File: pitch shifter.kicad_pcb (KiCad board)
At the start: 2 copper layers, 53.8 x 62.2 mm, 7 parts, among them J1 MOLEX_430450412, J2 MOLEX_436500315, U1 AP63200WU-7, U2 STM32G030K8T6, U3 PCM3060PWR, U4 LMV321LILT

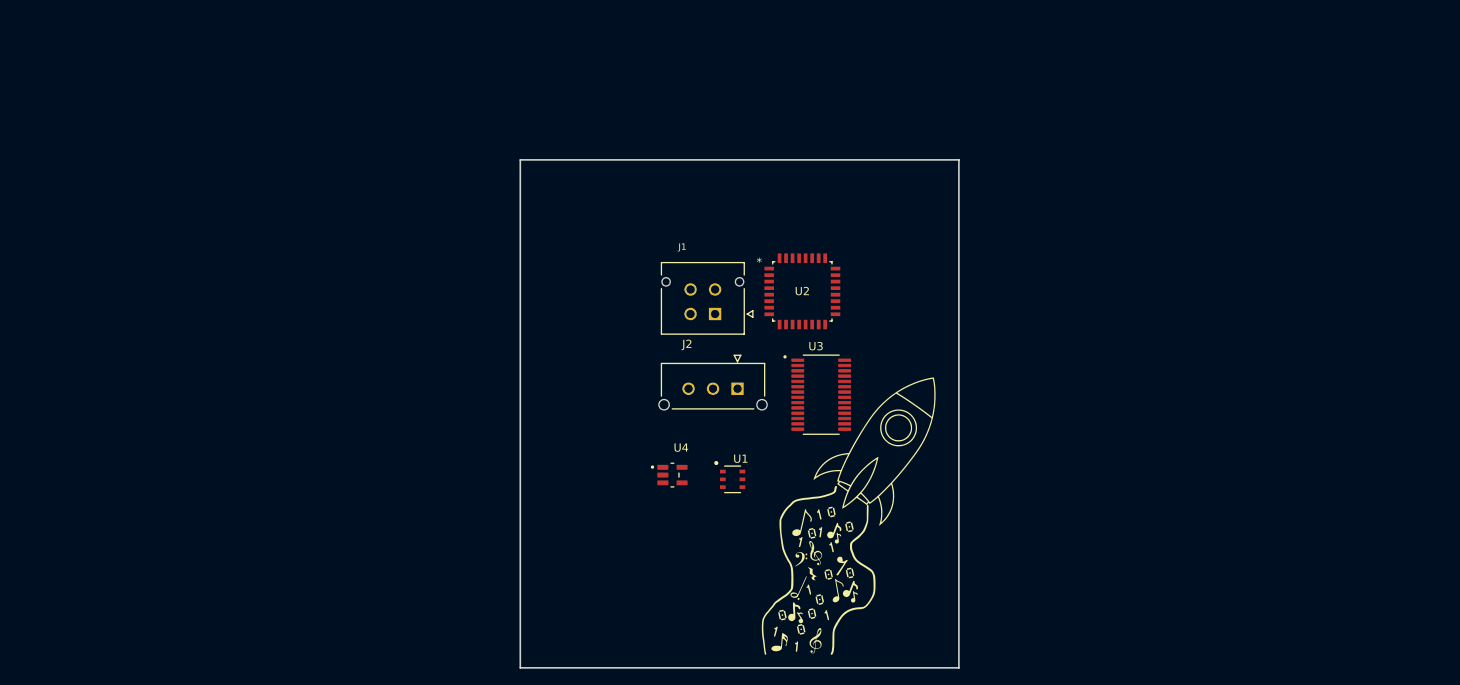
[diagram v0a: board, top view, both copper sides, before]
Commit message: Add oscillator, mounting holes, switches
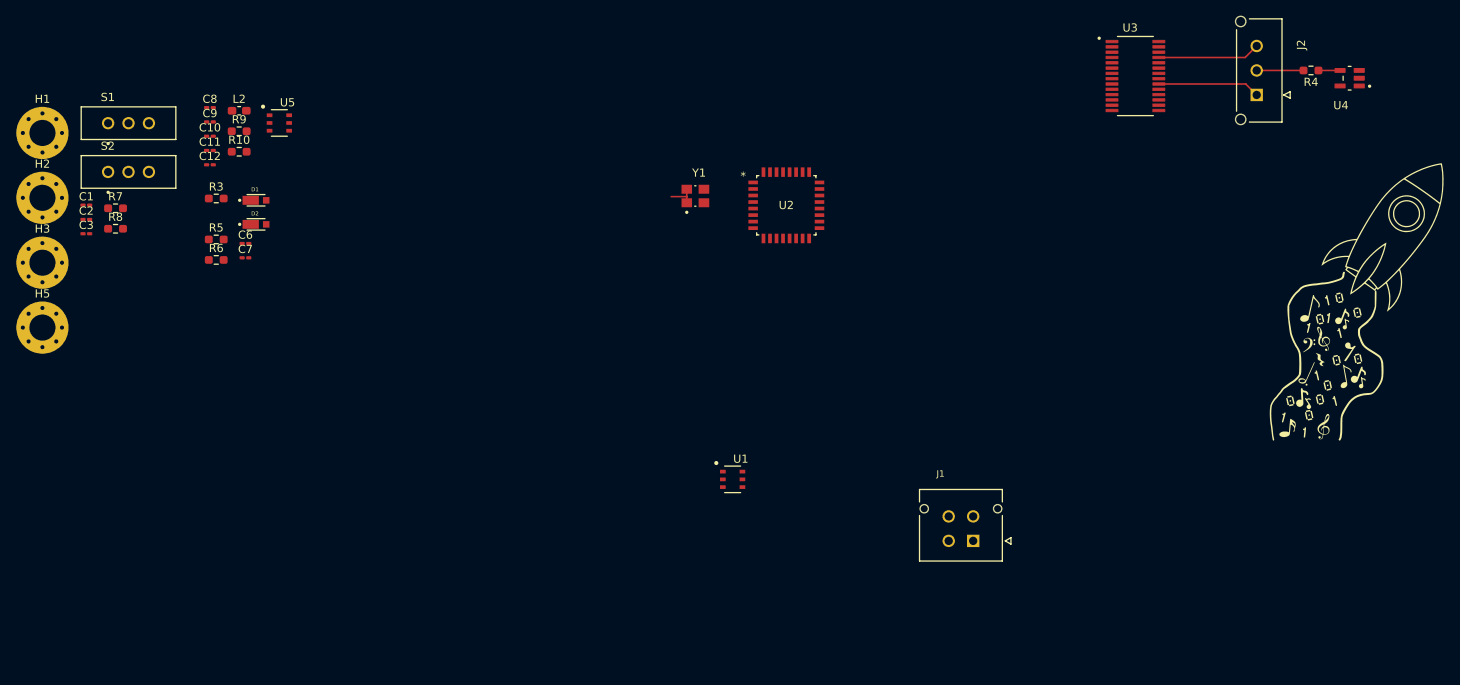
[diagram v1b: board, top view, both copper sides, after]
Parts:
- added C1: 100n, Capacitor_SMD:C_0201_0603Metric_Pad0.64x0.40mm_HandSolder, F.Cu at (64.6, 58.3)
- added C10: 100p, Capacitor_SMD:C_0201_0603Metric_Pad0.64x0.40mm_HandSolder, F.Cu at (79.7, 49.9)
- added C11: 22u, Capacitor_SMD:C_0201_0603Metric_Pad0.64x0.40mm_HandSolder, F.Cu at (79.7, 51.6)
- added C12: 22u, Capacitor_SMD:C_0201_0603Metric_Pad0.64x0.40mm_HandSolder, F.Cu at (79.7, 53.4)
- added C2: 100n, Capacitor_SMD:C_0201_0603Metric_Pad0.64x0.40mm_HandSolder, F.Cu at (64.6, 60.0)
- added C3: 100n, Capacitor_SMD:C_0201_0603Metric_Pad0.64x0.40mm_HandSolder, F.Cu at (64.6, 61.8)
- added C6: 100n, Capacitor_SMD:C_0201_0603Metric_Pad0.64x0.40mm_HandSolder, F.Cu at (84.1, 63.0)
- added C7: 100p, Capacitor_SMD:C_0201_0603Metric_Pad0.64x0.40mm_HandSolder, F.Cu at (84.1, 64.8)
- added C8: 10u, Capacitor_SMD:C_0201_0603Metric_Pad0.64x0.40mm_HandSolder, F.Cu at (79.7, 46.4)
- added C9: 100n, Capacitor_SMD:C_0201_0603Metric_Pad0.64x0.40mm_HandSolder, F.Cu at (79.7, 48.1)
- added D1: MSS1P4-M3_89A, Project_Components:MSS1P4-M3_89A, F.Cu at (85.4, 57.7)
- added D2: MSS1P4-M3_89A, Project_Components:MSS1P4-M3_89A, F.Cu at (85.4, 60.6)
- added H1: MountingHole_Pad, MountingHole:MountingHole_3.2mm_M3_Pad_Via, F.Cu at (59.2, 49.5)
- added H2: MountingHole_Pad, MountingHole:MountingHole_3.2mm_M3_Pad_Via, F.Cu at (59.2, 57.4)
- added H3: MountingHole_Pad, MountingHole:MountingHole_3.2mm_M3_Pad_Via, F.Cu at (59.2, 65.3)
- added H5: MountingHole_Pad, MountingHole:MountingHole_3.2mm_M3_Pad_Via, F.Cu at (59.2, 73.3)
- added L2: 6.8u, Inductor_SMD:L_0603_1608Metric_Pad1.05x0.95mm_HandSolder, F.Cu at (83.3, 46.7)
- added R10: 62K, Resistor_SMD:R_0603_1608Metric_Pad0.98x0.95mm_HandSolder, F.Cu at (83.3, 51.8)
- added R3: 100k, Resistor_SMD:R_0603_1608Metric_Pad0.98x0.95mm_HandSolder, F.Cu at (80.5, 57.5)
- added R4: 100k, Resistor_SMD:R_0603_1608Metric_Pad0.98x0.95mm_HandSolder, F.Cu at (214.6, 41.8)
- added R5: 10k, Resistor_SMD:R_0603_1608Metric_Pad0.98x0.95mm_HandSolder, F.Cu at (80.5, 62.5)
- added R6: 100k, Resistor_SMD:R_0603_1608Metric_Pad0.98x0.95mm_HandSolder, F.Cu at (80.5, 65.0)
- added R7: 10k, Resistor_SMD:R_0603_1608Metric_Pad0.98x0.95mm_HandSolder, F.Cu at (68.1, 58.7)
- added R8: 25, Resistor_SMD:R_0603_1608Metric_Pad0.98x0.95mm_HandSolder, F.Cu at (68.1, 61.2)
- added R9: 196K, Resistor_SMD:R_0603_1608Metric_Pad0.98x0.95mm_HandSolder, F.Cu at (83.3, 49.2)
- added S1: EG1218, Project_Components:EG1218, F.Cu at (69.7, 48.2)
- added S2: EG1218, Project_Components:EG1218, F.Cu at (69.7, 54.2)
- added U5: AP63200WU-7, Project_Components:AP63200WU_7, F.Cu at (88.2, 48.2)
- added Y1: ASE24LRT, Project_Components:ASE24LRT, F.Cu at (139.2, 57.5)
- moved U4 96.2 mm to (219.4, 42.7), turned to 180 degrees
- moved J2 73.1 mm to (208.0, 44.8), turned to -90 degrees
- moved G** 67.6 mm to (222.5, 67.2)
- moved U3 54.8 mm to (193.1, 42.5)
- moved J1 42.1 mm to (173.2, 99.4)
- moved U2 10.7 mm to (150.4, 58.3)
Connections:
- net /RST renamed /CRST
- J1 pad 3: /Voltage Regulator/VIN -> /Digital Voltage Regulator/VIN
- J2 pad 1: /GUITAR1 -> /GUITAR4
- J2 pad 3: /GUITAR4 -> /GUITAR1
- U2 pad 2: unconnected-(U2-PC14-OSC32_IN-Pad2) -> Net-(U2-PC14-OSC32_IN)
- U2 pad 25: unconnected-(U2-PA14-BOOT0-Pad25) -> Net-(U2-PA14-BOOT0)
- U2 pad 4: unconnected-(U2-VDD/VDDA-Pad4) -> /V3P3D
- U2 pad 6: unconnected-(U2-NRST-Pad6) -> Net-(U2-NRST)
- U3 pad 24: GND -> /V5A
- U3 pad 7: /V3P3 -> Net-(U3-VDD)
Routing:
- net /GUITAR1: track 0.00 -> 12.6 mm
- net /GUITAR4: track 0.00 -> 12.6 mm
- net /preamp/OUT: track 0.00 -> 5.74 mm
- net /V3P3D: track 0.00 -> 3.55 mm
- net Net-(C7-Pad1): track 0.00 -> 2.65 mm
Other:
- board outline removed
- copper layers 2 -> 4

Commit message: Began board layout
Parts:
- removed the C11 at (79.7, 51.6)
- removed the R10 at (83.3, 51.8)
- removed S1, S2: EG1218, Project_Components:EG1218
- removed the U2 at (150.4, 58.3)
- added C14: 10u, Capacitor_SMD:C_0603_1608Metric_Pad1.08x0.95mm_HandSolder, F.Cu at (139.0, 116.5)
- added C15: 10u, Capacitor_SMD:C_0603_1608Metric_Pad1.08x0.95mm_HandSolder, F.Cu at (156.8, 116.3)
- added C16: 100n, Capacitor_SMD:C_0603_1608Metric_Pad1.08x0.95mm_HandSolder, F.Cu at (133.0, 110.0)
- added C17: 100n, Capacitor_SMD:C_0603_1608Metric_Pad1.08x0.95mm_HandSolder, F.Cu at (150.8, 109.8)
- added C18: 100p, Capacitor_SMD:C_0603_1608Metric_Pad1.08x0.95mm_HandSolder, F.Cu at (135.8, 122.7)
- added C19: 100p, Capacitor_SMD:C_0603_1608Metric_Pad1.08x0.95mm_HandSolder, F.Cu at (153.7, 122.5)
- added C2: 100n, Capacitor_SMD:C_0603_1608Metric_Pad1.08x0.95mm_HandSolder, F.Cu at (131.5, 77.1)
- added C20: 22u, Capacitor_SMD:C_0603_1608Metric_Pad1.08x0.95mm_HandSolder, F.Cu at (141.0, 110.7)
- added C21: 22u, Capacitor_SMD:C_0603_1608Metric_Pad1.08x0.95mm_HandSolder, F.Cu at (158.9, 110.4)
- added C22: 22u, Capacitor_SMD:C_0603_1608Metric_Pad1.08x0.95mm_HandSolder, F.Cu at (138.5, 110.7)
- added C23: 22u, Capacitor_SMD:C_0603_1608Metric_Pad1.08x0.95mm_HandSolder, F.Cu at (156.4, 110.4)
- added C5: 100n, Capacitor_SMD:C_0603_1608Metric_Pad1.08x0.95mm_HandSolder, F.Cu at (141.9, 82.1)
- added C6: 100n, Capacitor_SMD:C_0603_1608Metric_Pad1.08x0.95mm_HandSolder, F.Cu at (204.2, 69.1)
- added C7: 10n, Capacitor_SMD:C_0603_1608Metric_Pad1.08x0.95mm_HandSolder, F.Cu at (134.5, 90.3)
- added D1: D, Diode_SMD:D_0603_1608Metric_Pad1.05x0.95mm_HandSolder, F.Cu at (186.1, 63.2)
- added J3: TBL002A-10, Project_Components:TBL002A-10, F.Cu at (86.0, 178.0)
- added J4: SBH11-PBPC-D05-ST-BK, Project_Components:SBH11-PBPC-D05-ST-BK, F.Cu at (117.7, 85.1)
- added L1: 10u, Inductor_SMD:L_0603_1608Metric_Pad1.05x0.95mm_HandSolder, F.Cu at (136.0, 108.3)
- added R1: 47, Resistor_SMD:R_0603_1608Metric_Pad0.98x0.95mm_HandSolder, F.Cu at (192.1, 59.6)
- added R11: 10k, Resistor_SMD:R_0603_1608Metric_Pad0.98x0.95mm_HandSolder, F.Cu at (185.8, 94.4)
- added R12: 10k, Resistor_SMD:R_0603_1608Metric_Pad0.98x0.95mm_HandSolder, F.Cu at (189.7, 94.4)
- added R15: 157k, Resistor_SMD:R_0603_1608Metric_Pad0.98x0.95mm_HandSolder, F.Cu at (135.9, 119.7)
- added R16: 30k, Resistor_SMD:R_0603_1608Metric_Pad0.98x0.95mm_HandSolder, F.Cu at (132.0, 116.7)
- added R17: 196K, Resistor_SMD:R_0603_1608Metric_Pad0.98x0.95mm_HandSolder, F.Cu at (153.8, 119.4)
- added R18: 62K, Resistor_SMD:R_0603_1608Metric_Pad0.98x0.95mm_HandSolder, F.Cu at (149.8, 116.5)
- added R4: 5.1k, Resistor_SMD:R_0603_1608Metric_Pad0.98x0.95mm_HandSolder, F.Cu at (143.7, 133.2)
- added R5: 47, Resistor_SMD:R_0603_1608Metric_Pad0.98x0.95mm_HandSolder, F.Cu at (190.8, 67.7)
- added R7: 4.7k, Resistor_SMD:R_0603_1608Metric_Pad0.98x0.95mm_HandSolder, F.Cu at (152.9, 84.3)
- added R8: 10k, Resistor_SMD:R_0603_1608Metric_Pad0.98x0.95mm_HandSolder, F.Cu at (143.8, 80.1)
- added SW3: PTS636, Project_Components:PTS636, F.Cu at (131.3, 73.6)
- added SW4: EG1218, Project_Components:EG1218, F.Cu at (143.7, 76.6)
- added TP1: Test Point, TestPoint:TestPoint_THTPad_D1.0mm_Drill0.5mm, F.Cu at (140.2, 130.8)
- added TP10: Test Point, TestPoint:TestPoint_THTPad_D1.0mm_Drill0.5mm, F.Cu at (239.0, 131.0)
- added TP11: Test Point, TestPoint:TestPoint_THTPad_D1.0mm_Drill0.5mm, F.Cu at (248.5, 118.3)
- added TP12: Test Point, TestPoint:TestPoint_THTPad_D1.0mm_Drill0.5mm, F.Cu at (248.5, 121.4)
- added TP13: Test Point, TestPoint:TestPoint_THTPad_D1.0mm_Drill0.5mm, F.Cu at (248.5, 124.5)
- added TP14: Test Point, TestPoint:TestPoint_THTPad_D1.0mm_Drill0.5mm, F.Cu at (248.5, 127.5)
- added TP15: Test Point, TestPoint:TestPoint_THTPad_D1.0mm_Drill0.5mm, F.Cu at (248.5, 130.6)
- added TP16: Test Point, TestPoint:TestPoint_THTPad_D1.0mm_Drill0.5mm, F.Cu at (256.6, 119.1)
- added TP17: Test Point, TestPoint:TestPoint_THTPad_D1.0mm_Drill0.5mm, F.Cu at (167.2, 96.8)
- added TP18: Test Point, TestPoint:TestPoint_THTPad_D1.0mm_Drill0.5mm, F.Cu at (256.6, 125.2)
- added TP19: Test Point, TestPoint:TestPoint_THTPad_D1.0mm_Drill0.5mm, F.Cu at (256.6, 128.3)
- added TP2: Test Point, TestPoint:TestPoint_THTPad_D1.0mm_Drill0.5mm, F.Cu at (151.8, 139.2)
- added TP20: Test Point, TestPoint:TestPoint_THTPad_D1.0mm_Drill0.5mm, F.Cu at (132.9, 97.3)
- added TP21: Test Point, TestPoint:TestPoint_THTPad_D1.0mm_Drill0.5mm, F.Cu at (135.9, 98.3)
- added TP22: Test Point, TestPoint:TestPoint_THTPad_D1.0mm_Drill0.5mm, F.Cu at (264.5, 121.4)
- added TP23: Test Point, TestPoint:TestPoint_THTPad_D1.0mm_Drill0.5mm, F.Cu at (264.5, 124.5)
- added TP24: Test Point, TestPoint:TestPoint_THTPad_D1.0mm_Drill0.5mm, F.Cu at (131.2, 93.8)
- added TP25: Test Point, TestPoint:TestPoint_THTPad_D1.0mm_Drill0.5mm, F.Cu at (264.5, 130.6)
- added TP26: Test Point, TestPoint:TestPoint_THTPad_D1.0mm_Drill0.5mm, F.Cu at (271.5, 118.9)
- added TP27: Test Point, TestPoint:TestPoint_THTPad_D1.0mm_Drill0.5mm, F.Cu at (271.5, 122.0)
- added TP28: Test Point, TestPoint:TestPoint_THTPad_D1.0mm_Drill0.5mm, F.Cu at (271.5, 125.0)
- added TP29: Test Point, TestPoint:TestPoint_THTPad_D1.0mm_Drill0.5mm, F.Cu at (271.5, 128.1)
- added TP3: Test Point, TestPoint:TestPoint_THTPad_D1.0mm_Drill0.5mm, F.Cu at (137.5, 139.2)
- added TP30: Test Point, TestPoint:TestPoint_THTPad_D1.0mm_Drill0.5mm, F.Cu at (271.5, 131.1)
- added TP31: Test Point, TestPoint:TestPoint_THTPad_D1.0mm_Drill0.5mm, F.Cu at (132.0, 120.7)
- added TP32: Test Point, TestPoint:TestPoint_THTPad_D1.0mm_Drill0.5mm, F.Cu at (130.5, 107.2)
- added TP33: Test Point, TestPoint:TestPoint_THTPad_D1.0mm_Drill0.5mm, F.Cu at (130.5, 113.2)
- added TP34: Test Point, TestPoint:TestPoint_THTPad_D1.0mm_Drill0.5mm, F.Cu at (138.6, 104.0)
- added TP35: Test Point, TestPoint:TestPoint_THTPad_D1.0mm_Drill0.5mm, F.Cu at (149.8, 120.4)
- added TP36: Test Point, TestPoint:TestPoint_THTPad_D1.0mm_Drill0.5mm, F.Cu at (148.3, 112.9)
- added TP37: Test Point, TestPoint:TestPoint_THTPad_D1.0mm_Drill0.5mm, F.Cu at (148.3, 106.9)
- added TP38: Test Point, TestPoint:TestPoint_THTPad_D1.0mm_Drill0.5mm, F.Cu at (156.5, 103.8)
- added TP4: Test Point, TestPoint:TestPoint_THTPad_D1.0mm_Drill0.5mm, F.Cu at (198.8, 69.2)
- added TP5: Test Point, TestPoint:TestPoint_THTPad_D1.0mm_Drill0.5mm, F.Cu at (53.8, 147.0)
- added TP6: Test Point, TestPoint:TestPoint_THTPad_D1.0mm_Drill0.5mm, F.Cu at (193.5, 98.5)
- added TP7: Test Point, TestPoint:TestPoint_THTPad_D1.0mm_Drill0.5mm, F.Cu at (239.0, 121.8)
- added TP8: Test Point, TestPoint:TestPoint_THTPad_D1.0mm_Drill0.5mm, F.Cu at (239.0, 124.9)
- added TP9: Test Point, TestPoint:TestPoint_THTPad_D1.0mm_Drill0.5mm, F.Cu at (239.0, 128.0)
- added U4: AP63200WU-7, Project_Components:AP63200WU_7, F.Cu at (136.0, 114.4)
- C1: renamed from C2; footprint Capacitor_SMD:C_0201_0603Metric_Pad0.64x0.40mm_HandSolder -> Capacitor_SMD:C_0603_1608Metric_Pad1.08x0.95mm_HandSolder
- C10: value 100p -> 4.7u; footprint Capacitor_SMD:C_0201_0603Metric_Pad0.64x0.40mm_HandSolder -> Capacitor_SMD:C_0603_1608Metric_Pad1.08x0.95mm_HandSolder
- C11: renamed from C6; value 100n -> 1u; footprint Capacitor_SMD:C_0201_0603Metric_Pad0.64x0.40mm_HandSolder -> Capacitor_SMD:C_0603_1608Metric_Pad1.08x0.95mm_HandSolder
- C12: value 22u -> 10u; footprint Capacitor_SMD:C_0201_0603Metric_Pad0.64x0.40mm_HandSolder -> Capacitor_SMD:C_0603_1608Metric_Pad1.08x0.95mm_HandSolder
- C13: renamed from C7; value 100p -> 1n; footprint Capacitor_SMD:C_0201_0603Metric_Pad0.64x0.40mm_HandSolder -> Capacitor_SMD:C_0603_1608Metric_Pad1.08x0.95mm_HandSolder
- C3: footprint Capacitor_SMD:C_0201_0603Metric_Pad0.64x0.40mm_HandSolder -> Capacitor_SMD:C_0603_1608Metric_Pad1.08x0.95mm_HandSolder
- C4: renamed from C1; footprint Capacitor_SMD:C_0201_0603Metric_Pad0.64x0.40mm_HandSolder -> Capacitor_SMD:C_0603_1608Metric_Pad1.08x0.95mm_HandSolder
- C8: value 10u -> 10n; footprint Capacitor_SMD:C_0201_0603Metric_Pad0.64x0.40mm_HandSolder -> Capacitor_SMD:C_0603_1608Metric_Pad1.08x0.95mm_HandSolder
- C9: value 100n -> 1u; footprint Capacitor_SMD:C_0201_0603Metric_Pad0.64x0.40mm_HandSolder -> Capacitor_SMD:C_0603_1608Metric_Pad1.08x0.95mm_HandSolder
- J1: value MOLEX_430450412 -> TBL002A-4; footprint Project_Components:MOLEX_430450412 -> Project_Components:TBL002A-4
- J2: value MOLEX_436500315 -> USB4125-GF-A; footprint Project_Components:MOLEX_436500315 -> Project_Components:USB-C (power only)
- R10: renamed from R6; value 100k -> 1k
- R13: renamed from R5; value 10k -> 4.7k
- R14: renamed from R4; value 100k -> 1k
- R2: renamed from R8; value 25 -> 47
- R3: value 100k -> 5.1k
- R9: value 196K -> 4.7k
- U1: value AP63200WU-7 -> STM32L432KCU6; footprint Project_Components:AP63200WU_7 -> Project_Components:STM32L432KCU6
- moved C1 131.6 mm to (196.1, 64.6)
- moved R2 131.6 mm to (199.7, 65.8)
- moved R6 131.6 mm to (199.7, 63.2)
- moved C12 114.2 mm to (187.9, 89.9)
- moved J2 114.0 mm to (144.4, 139.4), turned to 0 degrees
- moved R10 110.7 mm to (187.8, 91.9)
- moved J1 109.4 mm to (64.0, 93.0)
- moved C11 109.2 mm to (187.8, 97.1), turned to 90 degrees
- moved R13 105.4 mm to (183.2, 86.4)
- moved C3 104.4 mm to (164.9, 90.7), turned to -90 degrees
- moved C13 101.8 mm to (183.1, 88.1), turned to 180 degrees
- moved R3 99.6 mm to (145.2, 133.2), turned to 90 degrees
- moved D2 96.5 mm to (174.8, 94.1), turned to 90 degrees
- moved C4 95.5 mm to (153.2, 94.0), turned to -90 degrees
- moved L2 93.5 mm to (153.8, 108.0), turned to 90 degrees
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- renumbered D1 to D2, D2 to D3, H5 to H1, H1 to H2, H2 to H3, H3 to H4, R7 to R6, U3 to U2, U4 to U3
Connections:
- C10 pad 2: /Digital Voltage Regulator/FB -> GND
- C11 pad 1: /preamp/IN -> /JACK_IN
- C11 pad 2: Net-(C6-Pad2) -> Net-(C11-Pad2)
- C12 pad 1: /V3P3D -> Net-(C12-Pad1)
- C12 pad 2: GND -> Net-(C12-Pad2)
- C13 pad 2: Net-(C7-Pad2) -> Net-(C12-Pad1)
- C4 pad 1: Net-(U3-VDD) -> /V3P3D
- C8 pad 1: /Digital Voltage Regulator/VIN -> /V3P3D
- C9 pad 1: Net-(U5-BST) -> /V5A
- C9 pad 2: Net-(U5-SW) -> GND
- D2 pad 1: /preamp/VIN -> /V5A
- D2 pad 2: /preamp/OUT -> /OPAMP_OUT
- D3 pad 1: /preamp/OUT -> /OPAMP_OUT
- J1 pad 2: Net-(J1-Pad2) -> /VIN
- J1 pad 3: /Digital Voltage Regulator/VIN -> Net-(J1-Pad3)
- R10 pad 2: Net-(C7-Pad2) -> Net-(C12-Pad2)
- R13 pad 2: Net-(C7-Pad2) -> Net-(C12-Pad1)
- R14 pad 2: /preamp/OUT -> /OPAMP_OUT
- R2 pad 1: Net-(J1-Pad2) -> Net-(R2-Pad1)
- R3 pad 1: /preamp/VCOM -> Net-(J2-CC2)
- R3 pad 2: Net-(C6-Pad2) -> GND
- R9 pad 2: /Digital Voltage Regulator/FB -> /I2C_SDA
- U1 pad 1: /Voltage Regulator/FB -> /V3P3D
- U1 pad 2: /Voltage Regulator/VIN -> Net-(U1-PC14-OSC32_1N)
- U1 pad 3: /Voltage Regulator/VIN -> unconnected-(U1-PC15-OSC32_OUT-Pad3)
- U1 pad 4: GND -> /STRST
- U1 pad 5: Net-(U1-SW) -> /V5A
- U1 pad 6: Net-(U1-BST) -> /SYSCLK
- U2 pad 1: /I2C_SCL -> /I2C_SCLK
- U2 pad 4: /TIM3_CH1 -> /WSCLK
- U2 pad 5: /TIM3_CH2 -> /BLCK
- U2 pad 6: /TIM3_CH3 -> /SYSCLK
- U2 pad 7: Net-(U3-VDD) -> /V3P3D
- U3 pad 1: Net-(C6-Pad2) -> Net-(C11-Pad2)
- U3 pad 3: Net-(C7-Pad2) -> Net-(C12-Pad1)
- U3 pad 5: /preamp/VIN -> /V5A
- U5 pad 2: /Digital Voltage Regulator/VIN -> /VIN
- U5 pad 3: /Digital Voltage Regulator/VIN -> /VIN
- Y1 pad 3: Net-(U2-PC14-OSC32_IN) -> Net-(U1-PC14-OSC32_1N)
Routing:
- net GND: track 0.00 -> 63.6 mm, vias 0 -> 13
- net /V3P3D: track 3.55 -> 39.5 mm, vias 0 -> 3
- net /SYSCLK: track 0.00 -> 35.8 mm
- net /V5A: track 0.00 -> 34.0 mm, vias 0 -> 2
- net /BLCK: track 0.00 -> 33.7 mm, vias 0 -> 2
- net /CRST: track 0.00 -> 32.2 mm, vias 0 -> 2
- net /WSCLK: track 0.00 -> 30.9 mm, vias 0 -> 1
- net /STRST: track 0.00 -> 23.1 mm, vias 0 -> 2
- net /VSUP: track 0.00 -> 22.2 mm
- net /I2C_SDA: track 0.00 -> 19.9 mm
- net /I2C_SCLK: track 0.00 -> 19.0 mm, vias 0 -> 2
- net /GUITAR2: track 0.00 -> 15.8 mm
- net /GUITAR3: track 0.00 -> 13.8 mm, vias 0 -> 2
- net /Digital Voltage Regulator/FB: track 0.00 -> 13.1 mm
- net /Analog Voltage Regulator/FB: track 0.00 -> 13.1 mm
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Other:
- copper layers 4 -> 2
